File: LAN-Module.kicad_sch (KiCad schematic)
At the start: 93 parts, among them J1 USB_B_Micro, J10 ProtoCastellatedHeader, J11 ProtoCastellatedHeader, J12 ProtoCastellatedHeader, J13 ProtoCastellatedHeader, J14 ProtoCastellatedHeader, J15 ProtoCastellatedHeader, J16 ProtoCastellatedHeader, J17 ProtoCastellatedHeader, J18 ProtoCastellatedHeader, J19 ProtoCastellatedHeader, J2 HR911105A, J20 ProtoCastellatedHeader, J21 ProtoCastellatedHeader, J22 ProtoCastellatedHeader, J23 ProtoCastellatedHeader, J24 ProtoCastellatedHeader, J25 ProtoCastellatedHeader, J26 ProtoCastellatedHeader, J27 ProtoCastellatedHeader, J28 ProtoCastellatedHeader, J3 ProtoCastellatedHeader, J4 ProtoCastellatedHeader, J5 ProtoCastellatedHeader, J6 ProtoCastellatedHeader, J7 ProtoCastellatedHeader, J8 ProtoCastellatedHeader, J9 ProtoCastellatedHeader, Q1 2N7002, Q2 2N7002, SW1 RESET, U1 ESP32-U4WDH, U2 W25Q32, U3 LV2842XLVDDCR, U4 RTL8201F, U5 CP2102N-Axx-xQFN24, Y1 40MHz ±10ppm

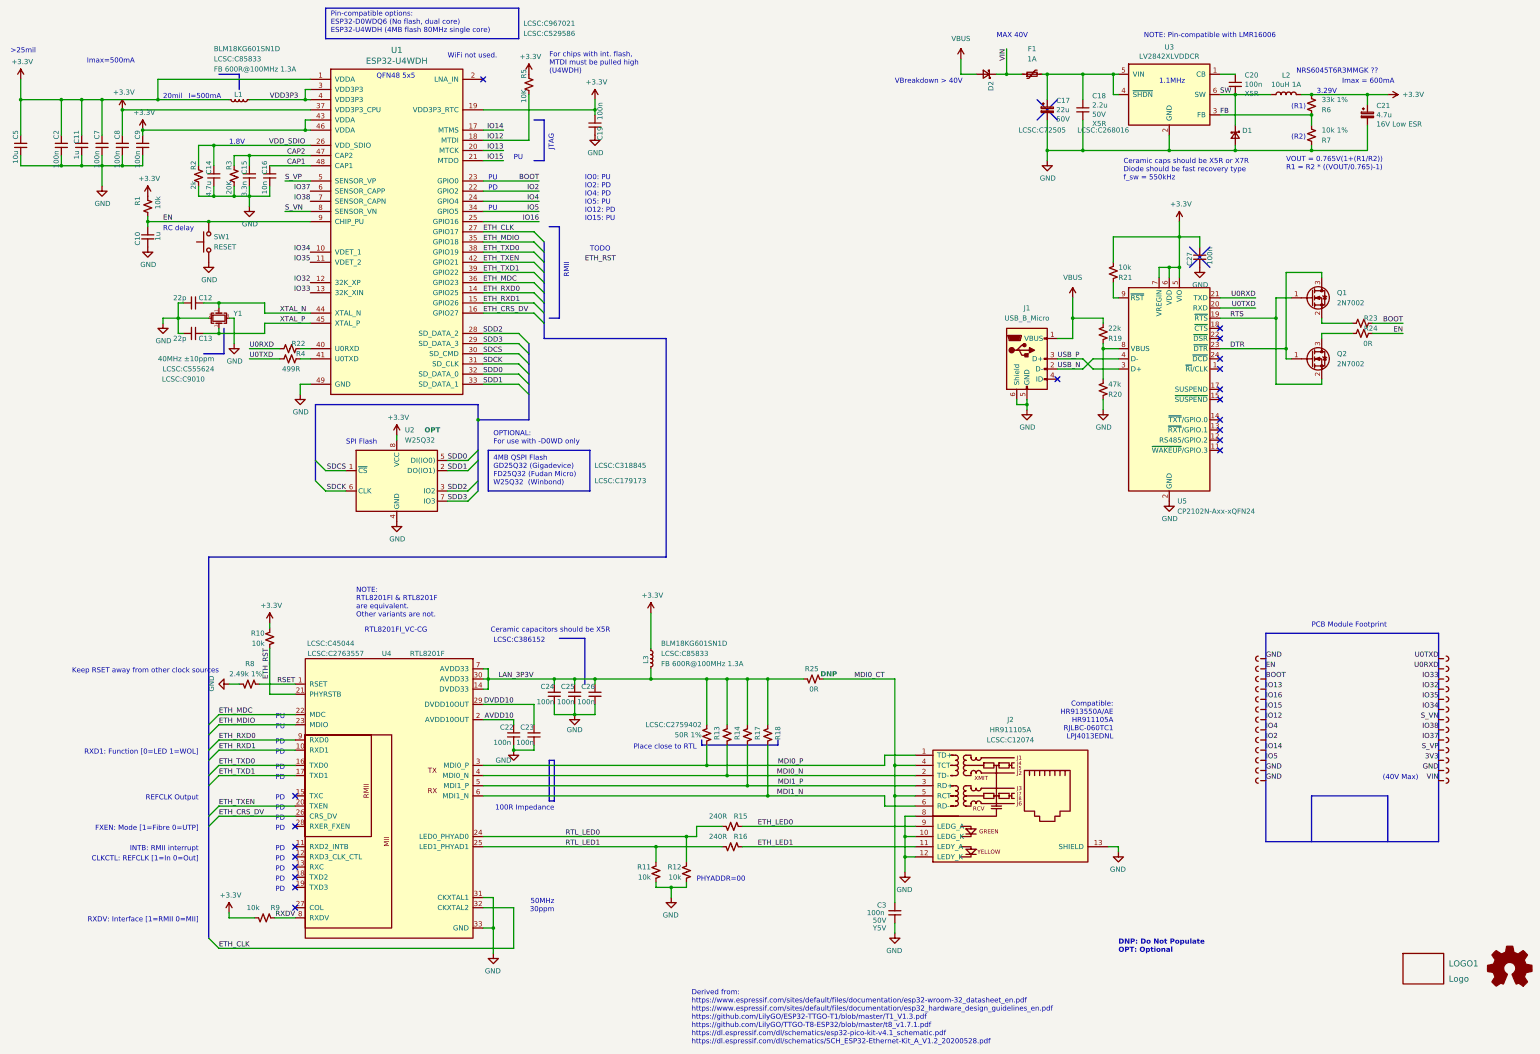
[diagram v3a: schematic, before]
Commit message: HW REV: Fix stability issue
Important change required to ensure stability across different types of ethernet switches.

I had only tested this with a TP-LINK switch, but the design did not work with other switches, and the reference schematic does NOT specify that the CT/termination resistors should be tied to 3.3V. Instead they should be coupled to GND through a capacitor (of unspecified value).
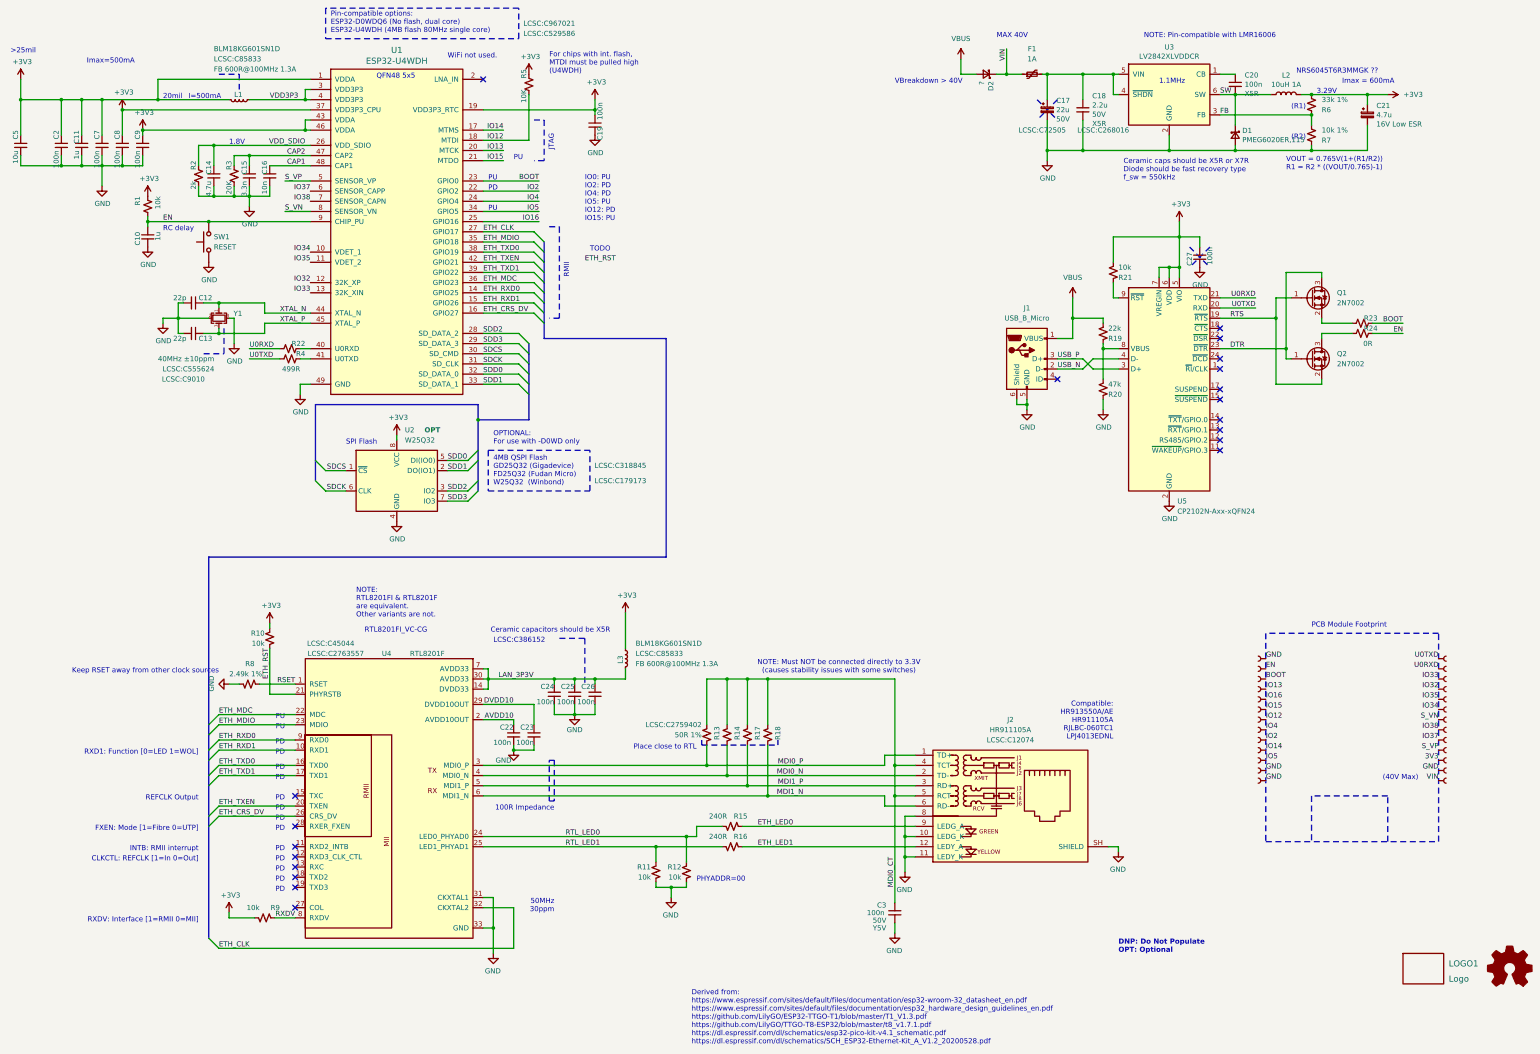
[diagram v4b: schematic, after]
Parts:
- removed R25: 0R, Resistor_SMD:R_0603_1608Metric, symbol EspGateway-rescue:R_Small_US-device-EspGateway-rescue
- D1: value (none) -> PMEG6020ER,115; footprint (none) -> Diode_SMD:D_SOD-123
- D2: value (none) -> ?
- J2: footprint Connector_RJ:RJ45_Hanrun_HR911105A -> Visclib:RJ45_Hanrun_HR911105A_Horizontal
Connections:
- net ETH_LED1: now also J2.12 (LEDY_A); no longer J2.11 (LEDY_A)
- net GND: now also J2.11 (LEDY_K), J2.SH (SHIELD); no longer J2.12 (LEDY_K), J2.13 (SHIELD)
- net LAN_3P3V: no longer R13.1, R14.1, R17.1, R18.1
- net MDI0_CT: now also R13.1, R14.1, R17.1, R18.1
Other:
- note added: "NOTE: Must NOT be connected directly to 3.3V (causes stability issues with some switches)"
- moved on the sheet: L3
